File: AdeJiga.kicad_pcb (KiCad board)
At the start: 2 copper layers, 72 x 72 mm, 33 parts, among them J1 Screw_Terminal_01x03, J10 Conn_01x02_Pin, J11 Conn_01x02_Pin, J2 Screw_Terminal_01x02, J3 Screw_Terminal_01x03, J4 Conn_01x05_Pin, J5 Conn_01x02_Pin, J6 Conn_01x03_Pin, J7 Conn_01x02_Pin, J8 Conn_01x03_Pin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

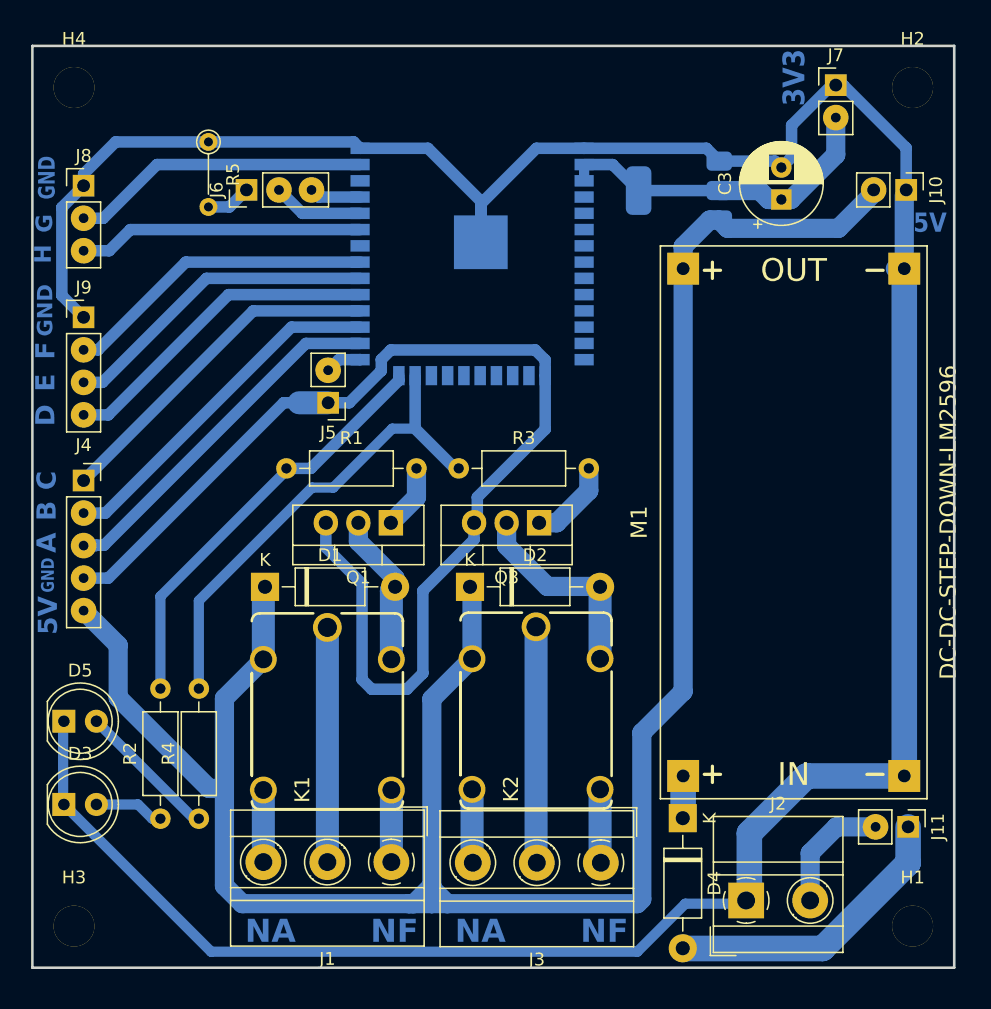
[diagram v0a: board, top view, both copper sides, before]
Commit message: Adicao dos modelos 3d e melhorias viasuais no layout
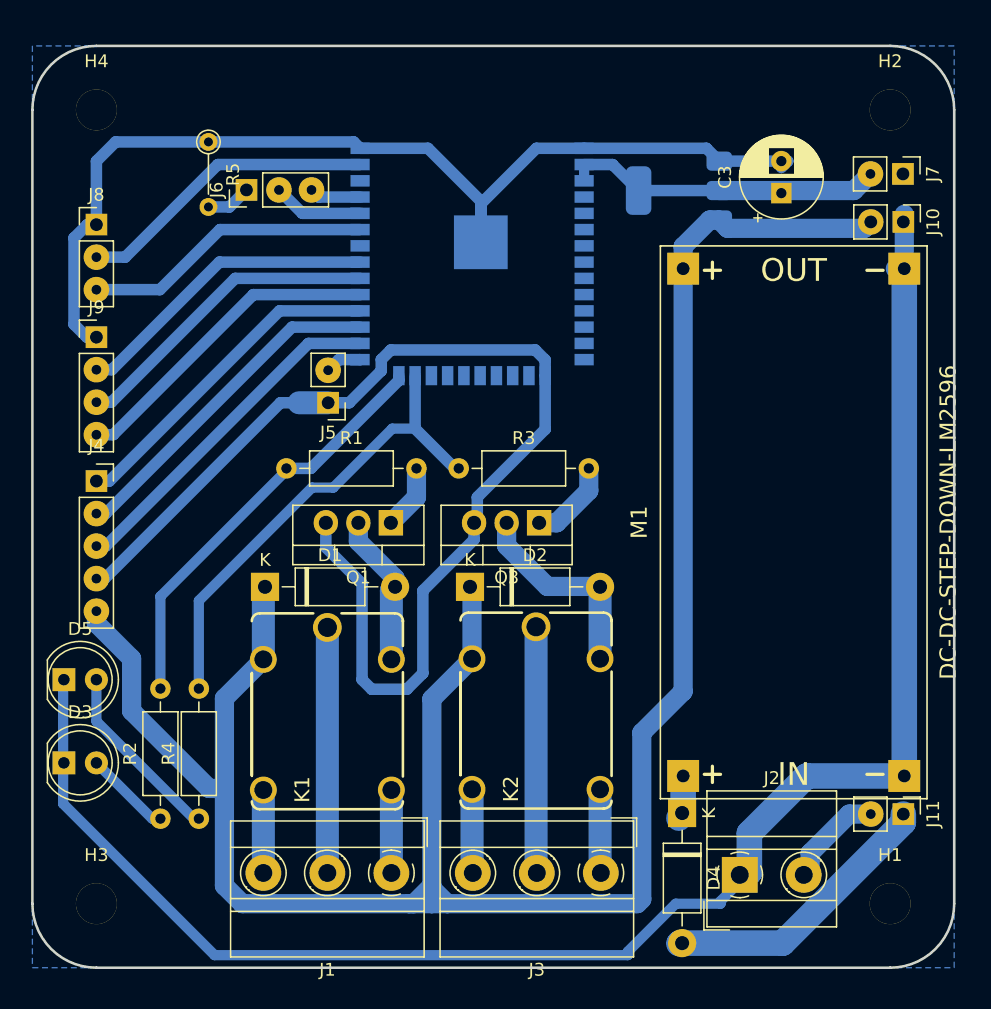
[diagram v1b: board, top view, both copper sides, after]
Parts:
- moved J7 8.70 mm to (190.0, 33.0), turned to -90 degrees
- moved D3 3.25 mm to (124.5, 79.0)
- moved D5 3.25 mm to (124.5, 72.5)
- moved J8 3.20 mm to (127.0, 37.0)
- moved J10 2.51 mm to (190.0, 36.8)
- moved H1 2.47 mm to (189.0, 90.0)
- moved H2 2.47 mm to (189.0, 28.0)
- moved H3 2.47 mm to (127.0, 90.0)
- moved H4 2.47 mm to (127.0, 28.0)
- moved J2 2.06 mm to (177.2, 87.8)
- moved J9 1.84 mm to (127.0, 45.8)
- moved J11 1.07 mm to (190.0, 83.0)
- moved J4 1.00 mm to (127.0, 57.0)
- moved J1 0.85 mm to (150.0, 87.6)
- moved J3 0.80 mm to (166.4, 87.6)
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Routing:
- net GND: track 321.2 -> 305.2 mm
- net Net-(D5-A): track 11.2 -> 13.9 mm
- net +5V: track 177.2 -> 175.3 mm
- net Net-(D3-A): track 5.21 -> 6.81 mm
- net Net-(J11-Pin_2): track 9.66 -> 8.10 mm
- net +3.3V: track 26.4 -> 25.0 mm
- net Net-(D4-A): track 23.2 -> 22.1 mm
- net GPIOC: track 27.1 -> 26.1 mm
- net GPIOB: track 27.6 -> 26.6 mm
- net GPIOA: track 28.1 -> 27.2 mm
- net Net-(J1-Pin_3): track 5.63 -> 6.43 mm
- net Net-(J1-Pin_2): track 18.3 -> 19.1 mm
- net Net-(J1-Pin_1): track 5.63 -> 6.43 mm
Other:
- outline, holes or cut-outs redrawn
- board text added: "-"
- board text removed: "GND"

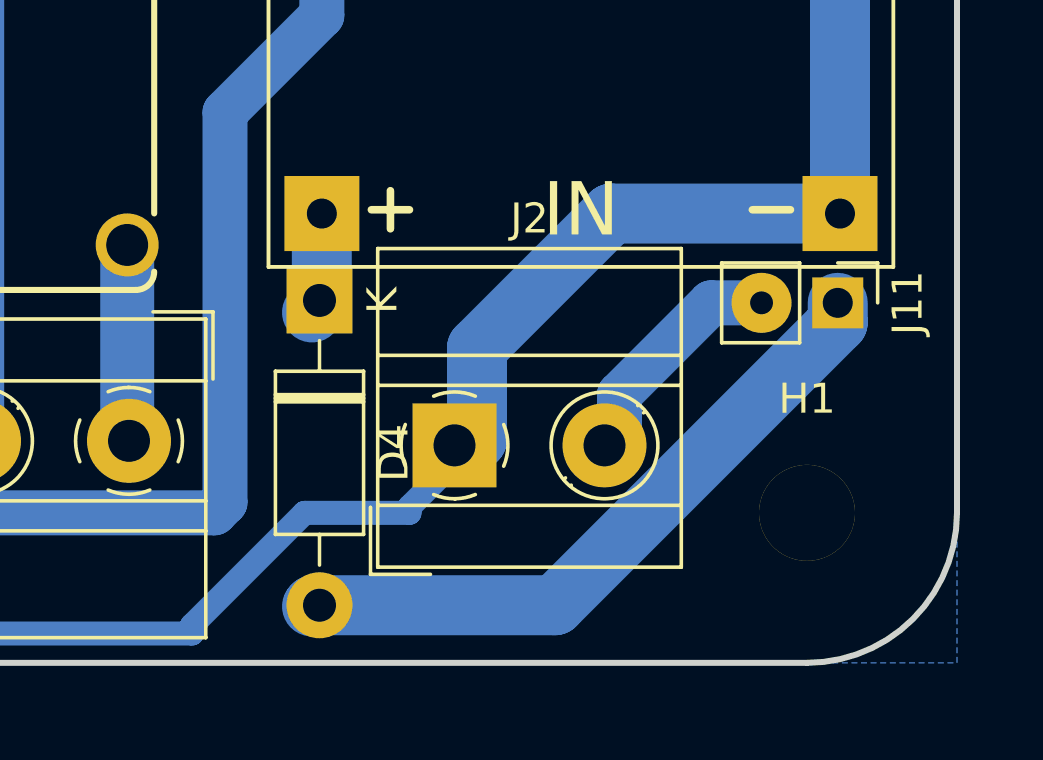
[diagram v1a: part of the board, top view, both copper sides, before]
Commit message: Atualização do modelo da tampa
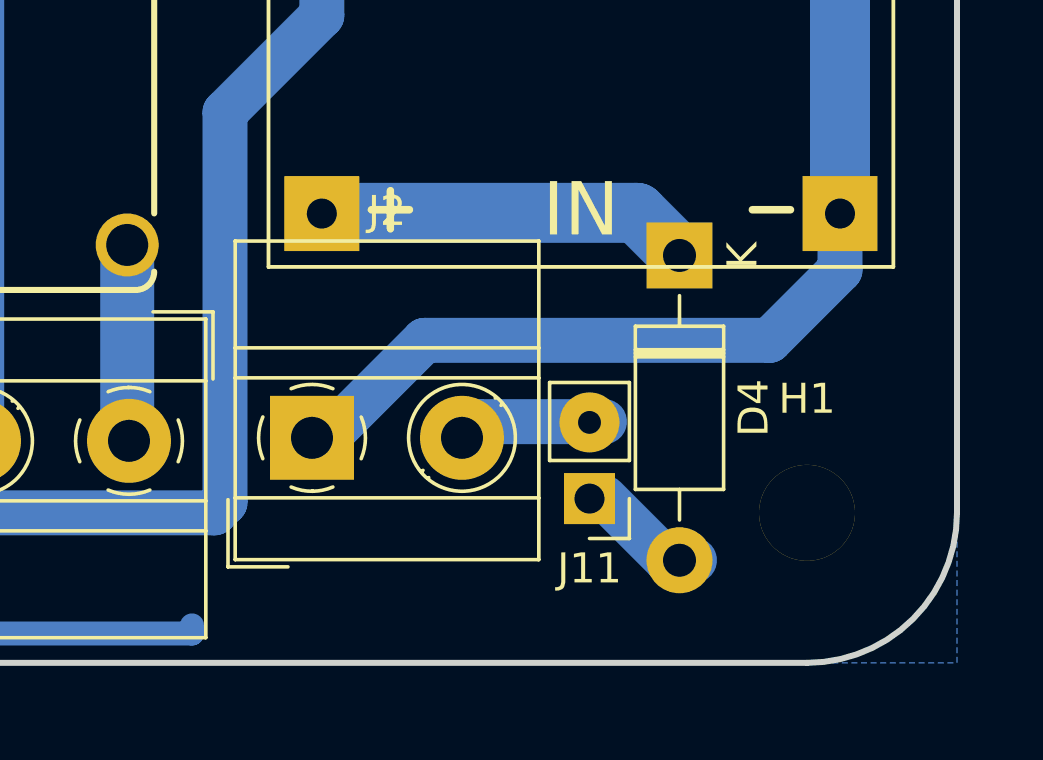
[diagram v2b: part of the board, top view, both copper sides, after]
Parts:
- moved D4 12.1 mm to (184.8, 81.4)
- moved J11 10.5 mm to (181.8, 89.5), turned to 180 degrees
- moved J2 4.76 mm to (172.5, 87.5)
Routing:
- net Net-(D4-A): track 22.1 -> 3.86 mm
- net +24V: track 3.43 -> 12.5 mm
- net GND: track 305.2 -> 297.3 mm
- net Net-(J11-Pin_2): track 8.10 -> 5.47 mm
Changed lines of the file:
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@@
 	(footprint "Diode_THT:D_DO-41_SOD81_P10.16mm_Horizontal"
 		(layer "F.Cu")
-		(at 172.75 82.92 -90)
+		(at 184.75 81.42 -90)
 		(descr "Diode, DO-41_SOD81 series, Axial, Horizontal, pin pitch=10.16mm, , length*diameter=5.2*2.7mm^2, , http://www.diodes.com/_files/packages/DO-41%20(Plastic).pdf")
 		(tags "Diode DO-41_SOD81 series Axial Horizontal pin pitch 10.16mm  length 5.2mm diameter 2.7mm")
@@
 	(footprint "TerminalBlock_MetzConnect:TerminalBlock_MetzConnect_Type011_RT05502HBWC_1x02_P5.00mm_Horizontal"
 		(layer "F.Cu")
-		(at 177.25 87.75)
+		(at 172.5 87.5)
 		(descr "terminal block Metz Connect Type011_RT05502HBWC, 2 pins, pitch 5mm, size 10x10.5mm^2, drill diamater 1.4mm, pad diameter 2.8mm, see http://www.metz-connect.com/de/system/files/productfiles/Datenblatt_310111_RT055xxHBLC_OFF-022717S.pdf, script-generated using https://github.com/pointhi/kicad-footprint-generator/scripts/TerminalBlock_MetzConnect")
 		(tags "THT terminal block Metz Connect Type011_RT05502HBWC pitch 5mm size 10x10.5mm^2 drill 1.4mm pad 2.8mm")
@@
 	(footprint "Connector_PinHeader_2.54mm:PinHeader_1x02_P2.54mm_Vertical"
 		(layer "F.Cu")
-		(at 190.025 83 -90)
+		(at 181.75 89.525 180)
 		(descr "Through hole straight pin header, 1x02, 2.54mm pitch, single row")
 		(tags "Through hole pin header THT 1x02 2.54mm single row")
 		(property "Reference" "J11"
-			(at 0 -2.33 90)
+			(at 0 -2.33 180)
 			(layer "F.SilkS")
 			(effects
@@
 		)
 		(property "Value" "Conn_01x02_Pin"
-			(at 0 4.87 90)
+			(at 0 4.87 180)
 			(layer "F.Fab")
 			(effects
@@
 		)
 		(property "Footprint" "Connector_PinHeader_2.54mm:PinHeader_1x02_P2.54mm_Vertical"
-			(at 0 0 -90)
+			(at 0 0 180)
 			(unlocked yes)
 			(layer "F.Fab")
@@
 		)
 		(property "Datasheet" ""
-			(at 0 0 -90)
+			(at 0 0 180)
 			(unlocked yes)
 			(layer "F.Fab")
@@
 		)
 		(property "Description" "Generic connector, single row, 01x02, script generated"
-			(at 0 0 -90)
+			(at 0 0 180)
 			(unlocked yes)
 			(layer "F.Fab")
@@
 		(attr through_hole)
 		(fp_line
-			(start -1.33 3.87)
+			(start 1.33 1.27)
 			(end 1.33 3.87)
 			(stroke
@@
 		)
 		(fp_line
-			(start -1.33 1.27)
-			(end -1.33 3.87)
+			(start -1.33 3.87)
+			(end 1.33 3.87)
 			(stroke
 				(width 0.12)
@@
 		)
 		(fp_line
-			(start 1.33 1.27)
-			(end 1.33 3.87)
+			(start -1.33 1.27)
+			(end -1.33 3.87)
 			(stroke
 				(width 0.12)
@@
 		)
 		(fp_line
-			(start -1.8 4.35)
-			(end 1.8 4.35)
+			(start 1.8 4.35)
+			(end 1.8 -1.8)
 			(stroke
 				(width 0.05)
@@
 		)
 		(fp_line
-			(start 1.8 4.35)
-			(end 1.8 -1.8)
+			(start 1.8 -1.8)
+			(end -1.8 -1.8)
 			(stroke
 				(width 0.05)
@@
 		)
 		(fp_line
-			(start -1.8 -1.8)
-			(end -1.8 4.35)
+			(start -1.8 4.35)
+			(end 1.8 4.35)
 			(stroke
 				(width 0.05)
@@
 		)
 		(fp_line
-			(start 1.8 -1.8)
-			(end -1.8 -1.8)
+			(start -1.8 -1.8)
+			(end -1.8 4.35)
 			(stroke
 				(width 0.05)
@@
 		)
 		(fp_line
-			(start -1.27 3.81)
-			(end -1.27 -0.635)
+			(start 1.27 3.81)
+			(end -1.27 3.81)
 			(stroke
 				(width 0.1)
@@
 		)
 		(fp_line
-			(start 1.27 3.81)
-			(end -1.27 3.81)
+			(start 1.27 -1.27)
+			(end 1.27 3.81)
 			(stroke
 				(width 0.1)
@@
 		)
 		(fp_line
-			(start -1.27 -0.635)
-			(end -0.635 -1.27)
+			(start -0.635 -1.27)
+			(end 1.27 -1.27)
 			(stroke
 				(width 0.1)
@@
 		)
 		(fp_line
-			(start -0.635 -1.27)
-			(end 1.27 -1.27)
+			(start -1.27 3.81)
+			(end -1.27 -0.635)
 			(stroke
 				(width 0.1)
@@
 		)
 		(fp_line
-			(start 1.27 -1.27)
-			(end 1.27 3.81)
+			(start -1.27 -0.635)
+			(end -0.635 -1.27)
 			(stroke
 				(width 0.1)
@@
 		)
 		(fp_text user "${REFERENCE}"
-			(at 0 1.27 180)
+			(at 0 1.27 -90)
 			(layer "F.Fab")
 			(effects
@@
 		)
 		(pad "1" thru_hole rect
-			(at 0 0 270)
+			(at 0 0 180)
 			(size 1.7 1.7)
 			(drill 1)
@@
 		)
 		(pad "2" thru_hole circle
-			(at 0 2.54 270)
+			(at 0 2.54 180)
 			(size 2 2)
 			(drill 0.762)
@@
 	)
 	(segment
-		(start 175.75 90)
-		(end 175.75 89.8)
-		(width 0.8)
+		(start 176.25 84.25)
+		(end 187.75 84.25)
+		(width 1.5)
 		(layer "B.Cu")
 		(net 2)
@@
 	)
 	(segment
-		(start 178 87.55)
-		(end 178 84.5)
-		(width 2)
-		(layer "B.Cu")
-		(net 2)
-	)
-	(segment
 		(start 156.75 60)
 		(end 156.5 60.25)
@@
 	)
 	(segment
-		(start 178 84.5)
-		(end 182.476 80.024)
-		(width 2)
-		(layer "B.Cu")
-		(net 2)
-	)
-	(segment
 		(start 144.92 62.17)
 		(end 144.92 60.25)
@@
 	)
 	(segment
+		(start 190.1 81.9)
+		(end 190.1 80.024)
+		(width 1.5)
+		(layer "B.Cu")
+		(net 2)
+	)
+	(segment
 		(start 124.4 72.56)
 		(end 124.4 82.19)
@@
 	)
 	(segment
-		(start 177.5 88.05)
-		(end 178 87.55)
-		(width 2)
-		(layer "B.Cu")
-		(net 2)
-	)
-	(segment
-		(start 175.75 89.8)
-		(end 177.5 88.05)
-		(width 0.8)
-		(layer "B.Cu")
-		(net 2)
-	)
-	(segment
 		(start 136.232136 94.022136)
 		(end 168.5 94.022136)
@@
 	)
 	(segment
-		(start 182.476 80.024)
-		(end 190.1 80.024)
-		(width 2)
+		(start 149.25 48.3725)
+		(end 146.7475 50.875)
+		(width 0.9)
 		(layer "B.Cu")
 		(net 2)
 	)
 	(segment
-		(start 149.25 48.3725)
-		(end 146.7475 50.875)
-		(width 0.9)
+		(start 187.75 84.25)
+		(end 190.1 81.9)
+		(width 1.5)
 		(layer "B.Cu")
 		(net 2)
@@
 	)
 	(segment
-		(start 156.5 60.25)
-		(end 156.5 61.554874)
-		(width 0.9)
+		(start 173 87.5)
+		(end 176.25 84.25)
+		(width 1.5)
 		(layer "B.Cu")
 		(net 2)
 	)
 	(segment
-		(start 172.25 90)
-		(end 175.75 90)
-		(width 0.8)
+		(start 156.5 60.25)
+		(end 156.5 61.554874)
+		(width 0.9)
 		(layer "B.Cu")
 		(net 2)
@@
 	)
 	(segment
-		(start 168.5 93.75)
-		(end 172.25 90)
-		(width 0.8)
-		(layer "B.Cu")
-		(net 2)
-	)
-	(segment
 		(start 125.25 44.75)
 		(end 125.25 38)
@@
 	)
 	(segment
-		(start 172.828 82.992)
-		(end 172.5 83.32)
+		(start 183.33 80)
+		(end 184.75 81.42)
 		(width 2)
 		(layer "B.Cu")
@@
 	(segment
 		(start 172.828 80.024)
-		(end 172.828 82.992)
+		(end 172.852 80)
 		(width 2)
 		(layer "B.Cu")
@@
 	)
 	(segment
-		(start 172.5 93.12)
-		(end 172.54 93.08)
-		(width 2)
-		(layer "B.Cu")
-		(net 6)
-	)
-	(segment
-		(start 180.596956 93.08)
-		(end 190.025 83.651956)
+		(start 172.852 80)
+		(end 183.33 80)
 		(width 2)
 		(layer "B.Cu")
-		(net 6)
+		(net 5)
 	)
 	(segment
-		(start 190.025 83.651956)
-		(end 190.025 83)
-		(width 2)
+		(start 184.33 91.58)
+		(end 182.25 89.5)
+		(width 1.5)
 		(layer "B.Cu")
 		(net 6)
 	)
 	(segment
-		(start 172.54 93.08)
-		(end 180.596956 93.08)
-		(width 2)
+		(start 185.25 91.58)
+		(end 184.33 91.58)
+		(width 1.5)
 		(layer "B.Cu")
 		(net 6)
@@
 	)
 	(segment
-		(start 182.75 87.8)
-		(end 182.75 86.05)
-		(width 1.5)
-		(layer "B.Cu")
-		(net 52)
-	)
-	(segment
-		(start 182.5 88.05)
-		(end 182.75 87.8)
+		(start 178.04 86.96)
+		(end 177.5 87.5)
 		(width 1.5)
 		(layer "B.Cu")
@@
 	)
 	(segment
-		(start 185.8 83)
-		(end 187.485 83)
+		(start 177.5 87.5)
+		(end 178 87.5)
 		(width 1.5)
 		(layer "B.Cu")
@@
 	)
 	(segment
-		(start 182.75 86.05)
-		(end 185.8 83)
+		(start 182.25 86.96)
+		(end 178.04 86.96)
 		(width 1.5)
 		(layer "B.Cu")

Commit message: 3 reles na jiga
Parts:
- added D6: 1N4007, Diode_THT:D_DO-41_SOD81_P10.16mm_Horizontal, F.Cu at (159.8, 71.0)
- added D7: LED, LED_THT:LED_D5.0mm_Clear, F.Cu at (165.8, 56.8)
- added J12: Screw_Terminal_01x03, TerminalBlock_MetzConnect:TerminalBlock_MetzConnect_Type011_RT05503HBWC_1x03_P5.00mm_Horizontal, F.Cu at (170.0, 93.2)
- added K3: JJM1C_relay, Benzlab:JJM1C_relay, F.Cu at (163.8, 80.5)
- added Q2: TIP127, Package_TO_SOT_THT:TO-220-3_Vertical, F.Cu at (161.5, 63.5)
- added R7: 220, Resistor_THT:R_Axial_DIN0207_L6.3mm_D2.5mm_P10.16mm_Horizontal, F.Cu at (171.0, 63.5)
- added R8: 3.3k, Resistor_THT:R_Axial_DIN0207_L6.3mm_D2.5mm_P10.16mm_Horizontal, F.Cu at (170.2, 66.8)
- moved R4 35.5 mm to (154.0, 53.4), turned to -90 degrees
- moved R2 30.2 mm to (137.2, 53.7), turned to -90 degrees
- moved D5 27.1 mm to (146.2, 56.4)
- moved D3 23.0 mm to (129.2, 56.5)
- moved Q1 22.4 mm to (127.8, 63.2), turned to 0 degrees
- moved Q3 17.5 mm to (144.4, 63.4), turned to 0 degrees
- moved J2 16.7 mm to (189.0, 89.8), turned to 90 degrees
- moved D1 15.1 mm to (126.2, 71.0)
- moved J1 15.1 mm to (136.0, 93.2)
- moved K1 15.1 mm to (131.0, 80.5)
- moved D2 14.5 mm to (142.8, 71.0)
- moved K2 14.5 mm to (148.0, 80.6)
- moved J3 14.5 mm to (153.0, 93.2)
- moved R1 11.9 mm to (136.2, 66.5), turned to 180 degrees
- moved H3 11.7 mm to (117.0, 96.0)
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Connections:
- net GPIO16 renamed REL1
- net GPIO17 renamed REL2
- U2 pad 16: unconnected-(U2-IO13-Pad16) -> REL3
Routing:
- net REL3: track 0.00 -> 29.2 mm
- net +5V: track 175.3 -> 202.5 mm
- net Net-(J12-Pin_2): track 0.00 -> 20.2 mm
- net Net-(D7-A): track 0.00 -> 16.0 mm
- net Ativa_Relé_3: track 0.00 -> 15.9 mm
- net REL2: track 38.2 -> 23.2 mm
- net GND: track 297.3 -> 283.2 mm
- net GPIOC: track 26.1 -> 36.9 mm
- net GPIOE: track 24.6 -> 35.1 mm
- net GPIOA: track 27.2 -> 37.7 mm
- net GPIOG: track 23.6 -> 34.1 mm
- net GPIOD: track 25.1 -> 35.6 mm
- net GPIOB: track 26.6 -> 37.1 mm
- net GPIOH: track 22.5 -> 33.0 mm
- net GPIOF: track 24.1 -> 34.6 mm
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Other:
- board size 72 x 72 mm -> 82 x 78 mm
